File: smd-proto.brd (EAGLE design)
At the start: 79.2 x 43.9 mm, 65 parts

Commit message: Added bunch of boards and outline
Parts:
- removed C10, C11, C12, C13, C14, C15, C16, C17, C18, C19, C20, C21, C3, C4, C5, C6, C7, C8, C9: 0.5PF 50V, Seeed-OPL-Capacitor:C0603
- removed C22, C23, C24, C25, C26, C27, C28, C29, C30, C31, C32, C33, C34, C35, C36, C37, C38, C39, C40: 2.2uf, Seeed-OPL-Capacitor:C0805
- added C41, C43, C45: 0.5PF 50V, Seeed-OPL-Capacitor:C0603
- added C42, C44, C46: 2.2uf, Seeed-OPL-Capacitor:C0805
- added D1, D2: RED-0805, Seeed-OPL-Diode:LED-0805
- added J1: GREEN-3P-5.0, Seeed-OPL-Connector:H3-5.0-15.5X8.0MM
- added JP15, JP17, JP19, JP20, JP27: (no value), SparkFun-Connectors:1X02
- added JP16: (no value), SparkFun-Connectors:1X09
- added JP18: FTDI_BASICPTH, SparkFun-Connectors:FTDI_BASIC
- added JP22, JP23, JP24, JP26, JP30, JP31: (no value), SparkFun-Connectors:1X08_NO_SILK
- added K1, K2: TS-1109-7, Seeed-OPL-Switch:SW4-6.2X6.2X5.0MM
- added R1, R3: 1.1M 1/10W, Seeed-OPL-Resistor:R0603
- added R2: 1K, Seeed-OPL-Resistor:R0603
- added U1: ATMEGA328P_PDIP, SparkFun-DigitalIC:DIL28-3
- added Y1: 16MHZ, Seeed-OPL-crystal-osctllator:X2-SMD-5.0X3.2X1.3MM
- C1: value 0.5PF 50V -> 22pf
- C2: value 2.2uf -> 22pf; device Seeed-OPL-Capacitor:C0805 -> Seeed-OPL-Capacitor:C0603
- JP10, JP9: device SparkFun-Connectors:1X01NS-KIT -> SparkFun-Connectors:1X14
- JP11: device SparkFun-Connectors:1X01NS-KIT -> SparkFun-Connectors:DB9_MALE
- JP12: device SparkFun-Connectors:1X01NS-KIT -> SparkFun-Connectors:1X09
- JP13: device SparkFun-Connectors:1X01NS-KIT -> SparkFun-Connectors:DB9
- JP4, JP6: device SparkFun-Connectors:1X01NS-KIT -> SparkFun-Connectors:1X02
- JP5: device SparkFun-Connectors:1X01NS-KIT -> SparkFun-Connectors:1X03
- JP7: value (none) -> RJ45; device SparkFun-Connectors:1X01NS-KIT -> SparkFun-Connectors:RJ45-8
- JP8: device SparkFun-Connectors:1X01NS-KIT -> SparkFun-Connectors:1X08_ROUND
- moved JP11 85.6 mm to (53.3, 83.8)
- moved JP13 82.7 mm to (15.7, 83.8)
- moved JP5 60.9 mm to (6.35, 61.7)
- moved JP12 56.3 mm to (43.4, 77.2)
- moved JP8 53.8 mm to (78.2, 17.8), turned to 180 degrees
- moved JP9 53.2 mm to (46.1, 50.9)
- moved JP7 47.3 mm to (69.3, 5.21)
- moved C1 43.6 mm to (60.5, 34.0), turned to 90 degrees
- moved C2 42.8 mm to (60.3, 32.3), flipped to the top, turned to 90 degrees
- moved JP6 33.8 mm to (2.03, 49.8)
- moved JP14 26.4 mm to (86.4, 8.64)
- moved JP10 19.7 mm to (46.1, 27.9)
- moved JP4 9.52 mm to (29.0, 21.1), turned to 270 degrees
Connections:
- removed net N$100: C35.2, C36.1
- removed net N$102: C18.1, C37.1, JP12.1
- removed net N$96: C13.2, C36.2, JP11.1
- removed net N$98: C33.2, C34.1
- removed net N$99: C34.2, C35.1
- new net A_A0: JP9.6, U1.23
- new net A_A1: JP9.5, U1.24
- new net A_A2: JP9.4, U1.25
- new net A_A3: JP9.3, U1.26
- new net A_A4/SDC: JP9.2, U1.27
- new net A_A5/SCL: JP9.1, U1.28
- new net A_AREF: JP10.13, U1.21
- new net A_D0/RX: JP10.4, U1.2
- new net A_D1/TX: JP10.5, U1.3
- new net A_D10~: JP9.13, U1.16
- new net A_D11~/MOSI: JP9.12, U1.17
- new net A_D2: JP10.6, U1.4
- new net A_D3~: JP10.7, U1.5
- new net A_D4: JP10.8, U1.6
- new net A_D5~: JP10.9, U1.11
- new net A_D6~: JP10.10, U1.12
- new net A_D7: JP10.11, U1.13
- new net A_D8: JP10.12, U1.14
- new net A_D9~: JP10.14, JP9.14, U1.15
- new net A_GND: C1.1, C2.1, JP10.2, JP9.9, U1.22, U1.8
- new net A_RESET: JP10.3, R2.2, U1.1
- new net A_VCC: JP10.1, JP9.8, R2.1, U1.20, U1.7
- new net D12/MISO: JP9.11, U1.18
- new net D13/SCK: JP9.10, U1.19
- new net FTDI_CTS: JP18.CTS
- new net FTDI_DTR: JP18.DTR
- new net FTDI_GND: JP18.GND
- new net FTDI_RX: JP18.RXI
- new net FTDI_TX: JP18.TXO
- new net FTDI_VCC: JP18.VCC
- new net N$108: JP27.2, R3.2
- new net N$43: C41.1, C42.1, JP15.1
- new net N$44: C41.2, C42.2, JP15.2
- new net N$45: C43.1, C44.1, JP17.1
- new net N$46: C43.2, C44.2, JP17.2
- new net N$47: C45.1, C46.1, JP19.1
- new net N$50: C45.2, C46.2, JP19.2
- new net N$52: JP4.2, K1.1, K1.4
- new net N$55: D1.+, JP6.1
- new net N$56: D1.-, R1.1
- new net N$76: JP11.1, JP12.1
- new net N$92: JP13.6, JP16.6
- net N$103: now also JP20.1, K2.2, K2.3; no longer C37.2, C38.1
- net N$104: now also JP20.2, K2.1, K2.4; no longer C38.2, C39.1
- net N$105: now also D2.+, JP27.1; no longer C39.2, C40.1
- net N$106: now also D2.-, R3.1; no longer C21.2, C40.2, JP13.1
- net N$41: now also JP4.1, K1.2, K1.3; no longer C3.2, C4.1
- net N$58: now also JP6.2, R1.2; no longer C4.2, C5.1
- net N$60: now also J1.2, JP5.2; no longer C1.2, C3.1
- net N$61: now also J1.1, JP5.1; no longer C10.1, C33.1, JP10.1
- net N$62: now also J1.3, JP5.3; no longer C6.2, C7.1
- net N$63: now also JP7.1, JP8.8; no longer C7.2, C8.1
- net N$64: now also JP7.2, JP8.7; no longer C8.2, C9.1
- net N$65: now also JP7.3, JP8.6; no longer C14.1, C29.1, JP8.1
- net N$66: now also JP7.4, JP8.5; no longer C17.2, C32.2, JP9.1
- net N$67: now also JP7.5, JP8.4; no longer C10.2, C11.1
- net N$68: now also JP7.6, JP8.3; no longer C11.2, C12.1
- net N$69: now also JP7.7, JP8.2; no longer C12.2, C13.1
- net N$72: now also JP7.8, JP8.1; no longer C14.2, C15.1
- net N$73: now also C1.2, U1.9, Y1.2; no longer C15.2, C16.1
- net N$74: now also C2.2, U1.10, Y1.1; no longer C16.2, C17.1
- net N$77: now also JP11.2, JP12.2; no longer C18.2, C19.1
- net N$78: now also JP11.3, JP12.3; no longer C19.2, C20.1
- net N$79: now also JP11.4, JP12.4; no longer C20.2, C21.1
- net N$82: now also JP11.5, JP12.5; no longer C1.1, C2.1, JP4.1
- net N$83: now also JP11.6, JP12.6; no longer C2.2, C22.1
- net N$84: now also JP11.7, JP12.7; no longer C22.2, C23.1
- net N$85: now also JP11.8, JP12.8; no longer C23.2, C24.1
- net N$86: now also JP11.9, JP12.9; no longer C24.2, C5.2, JP5.1
- net N$87: now also JP13.1, JP16.1; no longer C25.1, C6.1, JP6.1
- net N$88: now also JP13.2, JP16.2; no longer C25.2, C26.1
- net N$89: now also JP13.3, JP16.3; no longer C26.2, C27.1
- net N$90: now also JP13.4, JP16.4; no longer C27.2, C28.1
- net N$91: now also JP13.5, JP16.5; no longer C28.2, C9.2, JP7.1
- net N$93: now also JP13.7, JP16.7; no longer C29.2, C30.1
- net N$94: now also JP13.8, JP16.8; no longer C30.2, C31.1
- net N$95: now also JP13.9, JP16.9; no longer C31.2, C32.1
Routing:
- net A_VCC: track 0.00 -> 46.4 mm
- net A_GND: track 0.00 -> 39.5 mm, vias 0 -> 1
- net A_AREF: track 0.00 -> 26.3 mm
- net N$76: track 0.00 -> 21.3 mm
- net N$86: track 5.97 -> 23.2 mm
- net N$85: track 2.79 -> 18.2 mm
- net N$77: track 2.54 -> 17.3 mm
- net A_D5~: track 0.00 -> 13.2 mm
- net N$84: track 2.79 -> 15.9 mm
- net A_D3~: track 0.00 -> 11.7 mm
- net A_D8: track 0.00 -> 11.6 mm
- net A_D6~: track 0.00 -> 11.6 mm
- net A_D2: track 0.00 -> 11.5 mm
- net A_D1/TX: track 0.00 -> 11.5 mm
- net A_RESET: track 0.00 -> 11.5 mm
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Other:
- board size 79.2 x 43.9 mm -> 94.2 x 91.2 mm
- board text added: "A0"
- board text added: "A1"
- board text added: "A2"
- board text added: "A3"
- board text added: "A4"
- board text added: "A5"
- board text added: "AREF"
- board text added: "BLUE"
- board text added: "BRN"
- board text added: "CTS"
- board text added: "D0"
- board text added: "D1"
- board text added: "D10~"
- board text added: "D11~"
- board text added: "D12"
- board text added: "D13"
- board text added: "D2"
- board text added: "D3~"
- board text added: "D4"
- board text added: "D5~"
- board text added: "D6~"
- board text added: "D7"
- board text added: "D8"
- board text added: "DB9 FEMALE BREAKOUT"
- board text added: "DB9 MALE BREAKOUT"
- board text added: "DTR"
- board text added: "FTDI ADAPTER"
- board text added: "GRN"
- board text added: "ORG"
- board text added: "RJ45-breakout"
- board text added: "RX"
- board text added: "SIGNAL"
- board text added: "TX"
- board text added: "W/BLUE"
- board text added: "W/BRN"
- board text added: "W/GRN"
- board text added: "W/ORG"
- board text removed: "0603"
- board text removed: "0805"

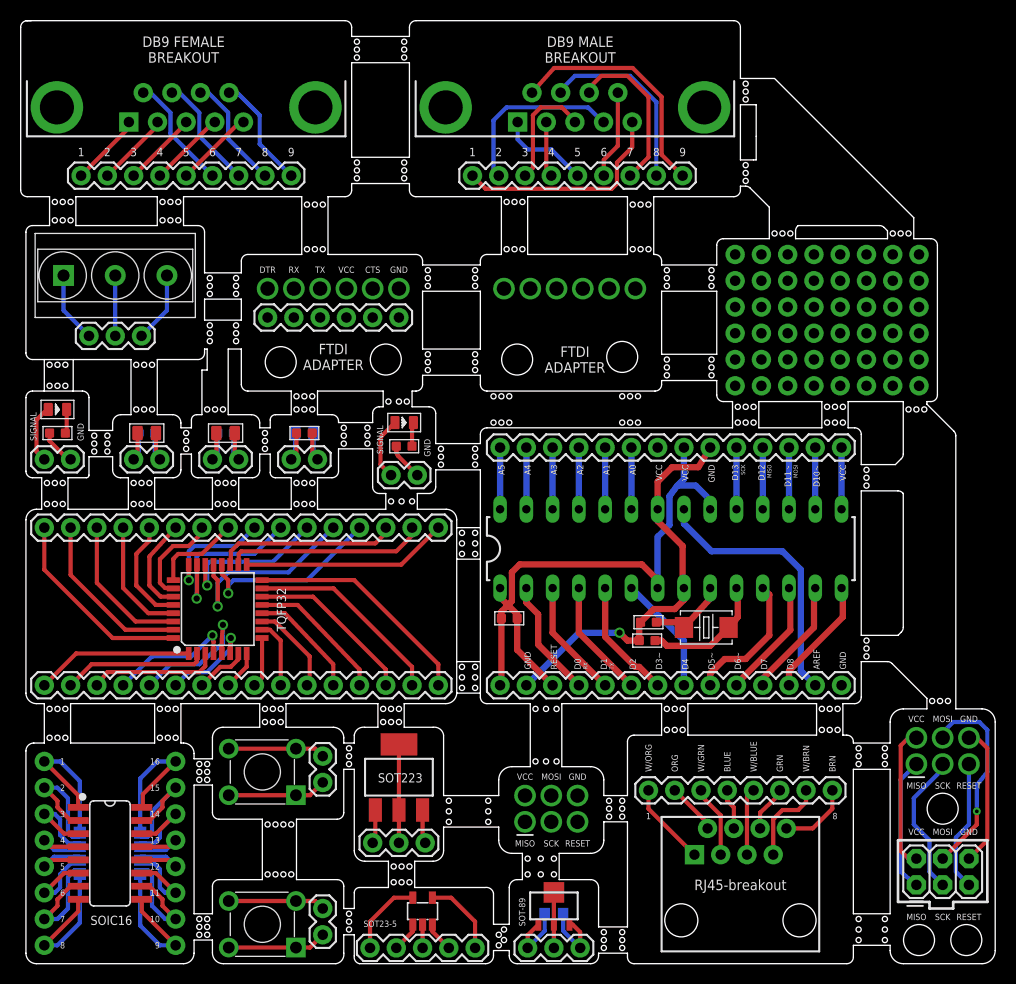
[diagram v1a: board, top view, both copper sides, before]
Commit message: Fixed ERC and DRC issues, finalized some boards
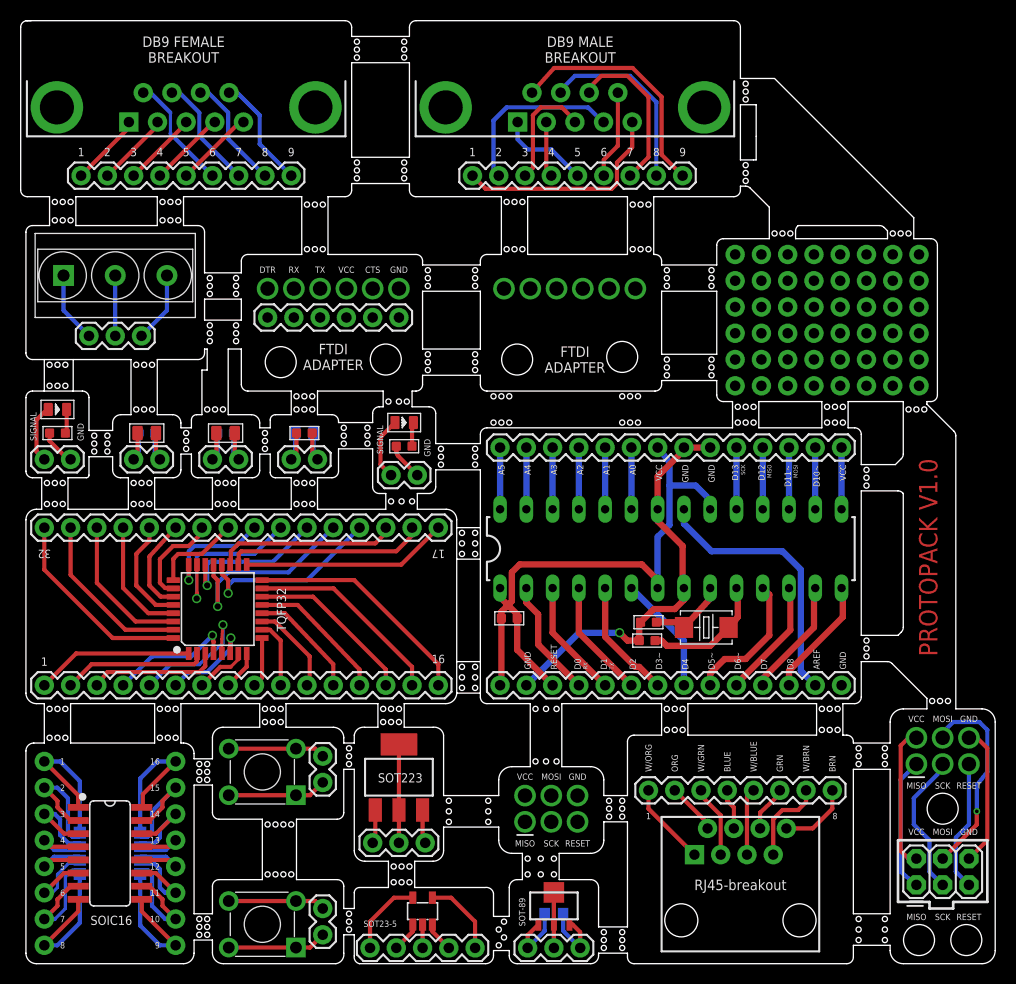
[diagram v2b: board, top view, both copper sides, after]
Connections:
- net A_GND: now also JP9.8
- net A_VCC: now also JP9.7; no longer JP9.8
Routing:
- net A_VCC: track 46.4 -> 47.1 mm
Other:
- outline, holes or cut-outs redrawn
- board text added: "17"
- board text added: "32"
- board text added: "PROTOPACK V1.0"
